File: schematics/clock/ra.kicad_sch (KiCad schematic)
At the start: 19 parts, among them U7 74LS173, U8 74LS173, U9 74LS245

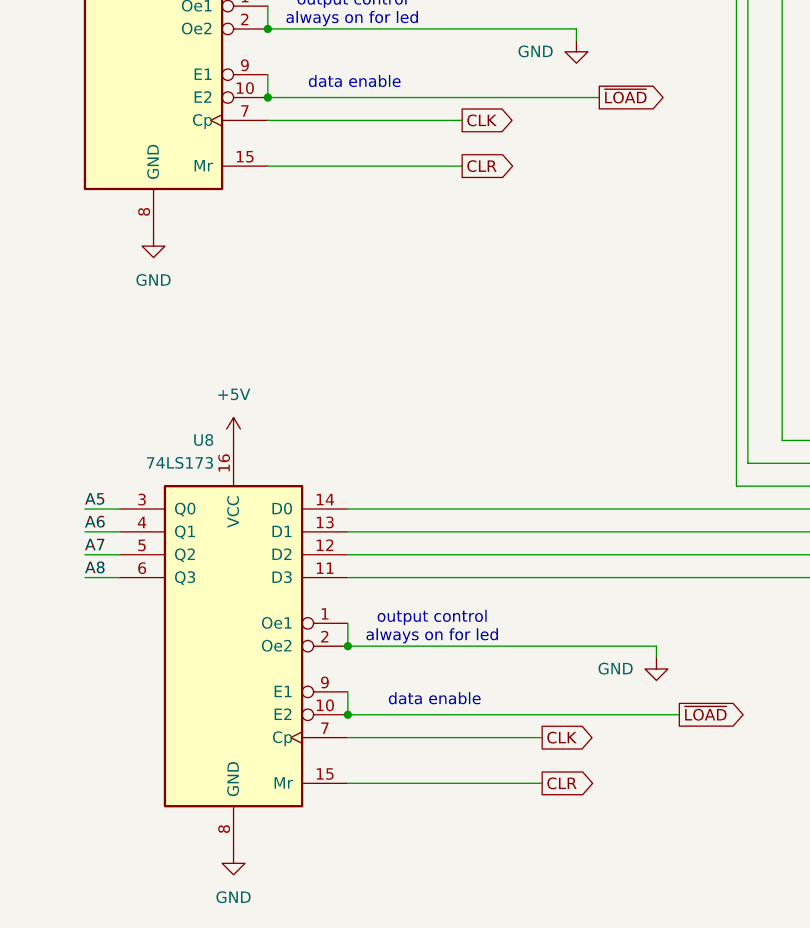
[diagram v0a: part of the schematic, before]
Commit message: ground clear
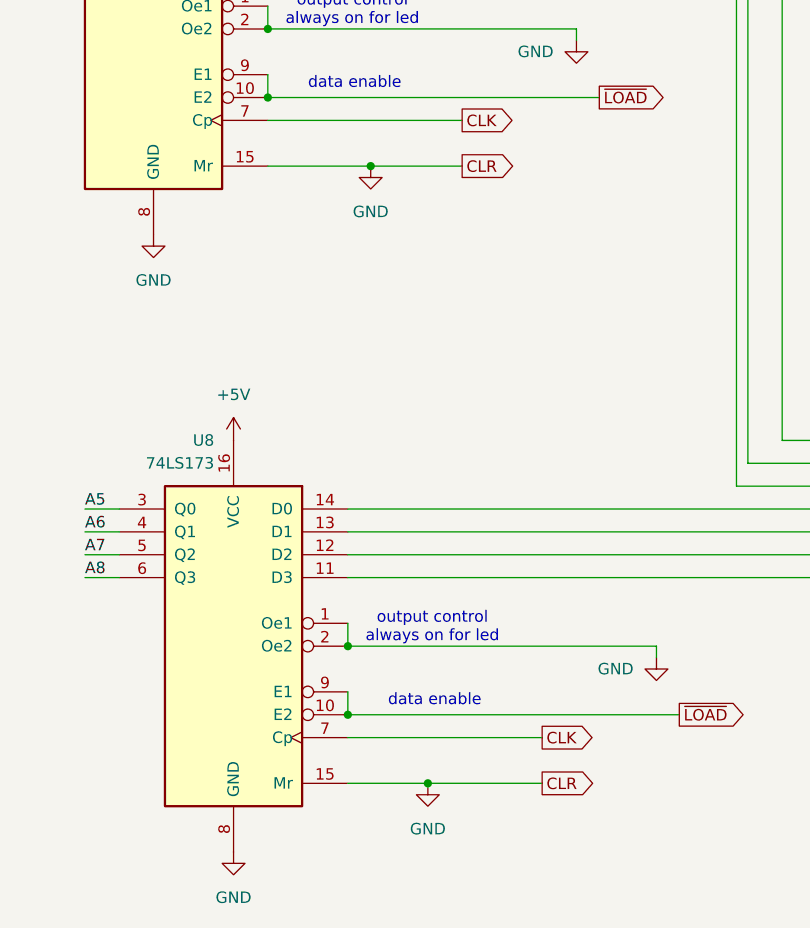
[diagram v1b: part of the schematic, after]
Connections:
- net CLR is gone; now on net GND: U7.15 (Mr), U8.15 (Mr)
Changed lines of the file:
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@@
 	)
 	(junction
+		(at 105.41 77.47)
+		(diameter 0)
+		(color 0 0 0 0)
+	)
+	(junction
 		(at 172.72 118.11)
 		(diameter 0)
@@
 	)
 	(junction
+		(at 111.76 146.05)
+		(diameter 0)
+		(color 0 0 0 0)
+	)
+	(junction
 		(at 185.42 60.96)
 		(diameter 0)
@@
 	(wire
 		(pts
+			(xy 111.76 146.05) (xy 102.87 146.05)
+		)
+		(stroke
+			(width 0)
+			(type default)
+		)
+	)
+	(wire
+		(pts
 			(xy 64.77 49.53) (xy 68.58 49.53)
 		)
@@
 	(wire
 		(pts
-			(xy 115.57 77.47) (xy 93.98 77.47)
+			(xy 115.57 77.47) (xy 105.41 77.47)
 		)
 		(stroke
@@
 	(wire
 		(pts
+			(xy 105.41 77.47) (xy 93.98 77.47)
+		)
+		(stroke
+			(width 0)
+			(type default)
+		)
+	)
+	(wire
+		(pts
 			(xy 179.07 60.96) (xy 185.42 60.96)
 		)
@@
 	(wire
 		(pts
-			(xy 124.46 146.05) (xy 102.87 146.05)
+			(xy 124.46 146.05) (xy 111.76 146.05)
 		)
 		(stroke
@@
 	)
 	(symbol
+		(lib_id "power:GND")
+		(at 111.76 146.05 0)
+		(unit 1)
+		(exclude_from_sim no)
+		(in_bom yes)
+		(on_board yes)
+		(dnp no)
+		(fields_autoplaced yes)
+		(property "Reference" "#PWR041"
+			(at 111.76 152.4 0)
+			(effects
+				(font
+					(size 1.27 1.27)
+				)
+				(hide yes)
+			)
+		)
+		(property "Value" "GND"
+			(at 111.76 151.13 0)
+			(effects
+				(font
+					(size 1.27 1.27)
+				)
+			)
+		)
+		(property "Footprint" ""
+			(at 111.76 146.05 0)
+			(effects
+				(font
+					(size 1.27 1.27)
+				)
+				(hide yes)
+			)
+		)
+		(property "Datasheet" ""
+			(at 111.76 146.05 0)
+			(effects
+				(font
+					(size 1.27 1.27)
+				)
+				(hide yes)
+			)
+		)
+		(property "Description" "Power symbol creates a global label with name \"GND\" , ground"
+			(at 111.76 146.05 0)
+			(effects
+				(font
+					(size 1.27 1.27)
+				)
+				(hide yes)
+			)
+		)
+		(pin "1"
+		)
+		(instances
+			(project "clock"
+				(path "/1be175cd-1437-4d72-8152-541f02e1a99b/d58d7b4b-c7c9-4a9b-82e5-f70bb60ff1ca/3d0a87ec-a2f4-438c-aa57-9e074d6f2ca0"
+					(reference "#PWR041")
+					(unit 1)
+				)
+			)
+		)
+	)
+	(symbol
 		(lib_id "Device:LED")
 		(at 179.07 78.74 270)
@@
 					(unit 1)
 				)
+			)
+		)
+	)
+	(symbol
+		(lib_id "power:GND")
+		(at 105.41 77.47 0)
+		(unit 1)
+		(exclude_from_sim no)
+		(in_bom yes)
+		(on_board yes)
+		(dnp no)
+		(fields_autoplaced yes)
+		(property "Reference" "#PWR040"
+			(at 105.41 83.82 0)
+			(effects
+				(font
+					(size 1.27 1.27)
+				)
+				(hide yes)
+			)
+		)
+		(property "Value" "GND"
+			(at 105.41 82.55 0)
+			(effects
+				(font
+					(size 1.27 1.27)
+				)
+			)
+		)
+		(property "Footprint" ""
+			(at 105.41 77.47 0)
+			(effects
+				(font
+					(size 1.27 1.27)
+				)
+				(hide yes)
+			)
+		)
+		(property "Datasheet" ""
+			(at 105.41 77.47 0)
+			(effects
+				(font
+					(size 1.27 1.27)
+				)
+				(hide yes)
+			)
+		)
+		(property "Description" "Power symbol creates a global label with name \"GND\" , ground"
+			(at 105.41 77.47 0)
+			(effects
+				(font
+					(size 1.27 1.27)
+				)
+				(hide yes)
+			)
+		)
+		(pin "1"
+		)
+		(instances
+			(project "clock"
+				(path "/1be175cd-1437-4d72-8152-541f02e1a99b/d58d7b4b-c7c9-4a9b-82e5-f70bb60ff1ca/3d0a87ec-a2f4-438c-aa57-9e074d6f2ca0"
+					(reference "#PWR040")
+					(unit 1)
+				)

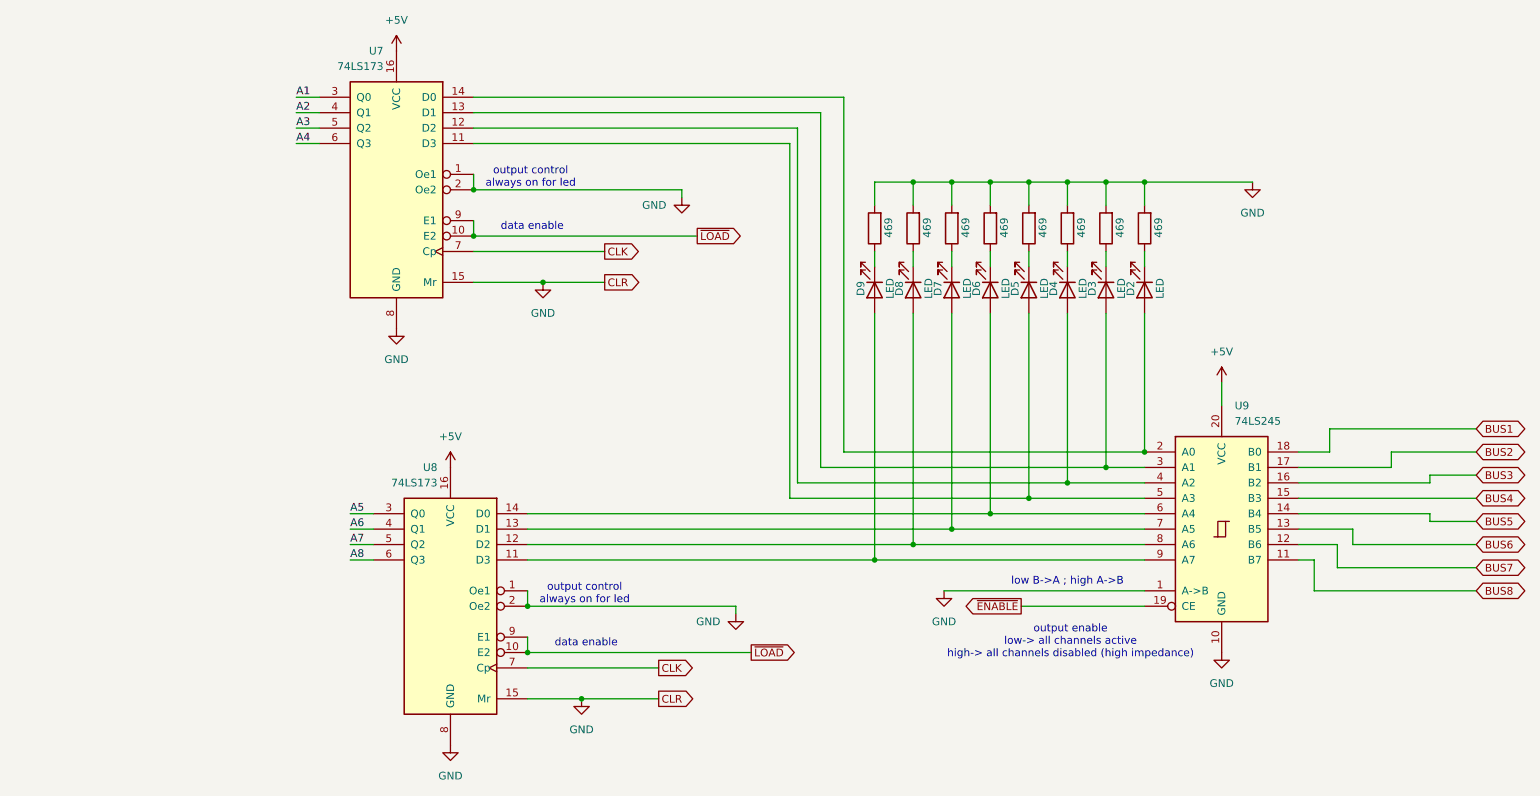
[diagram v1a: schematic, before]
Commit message: swap led position on registers
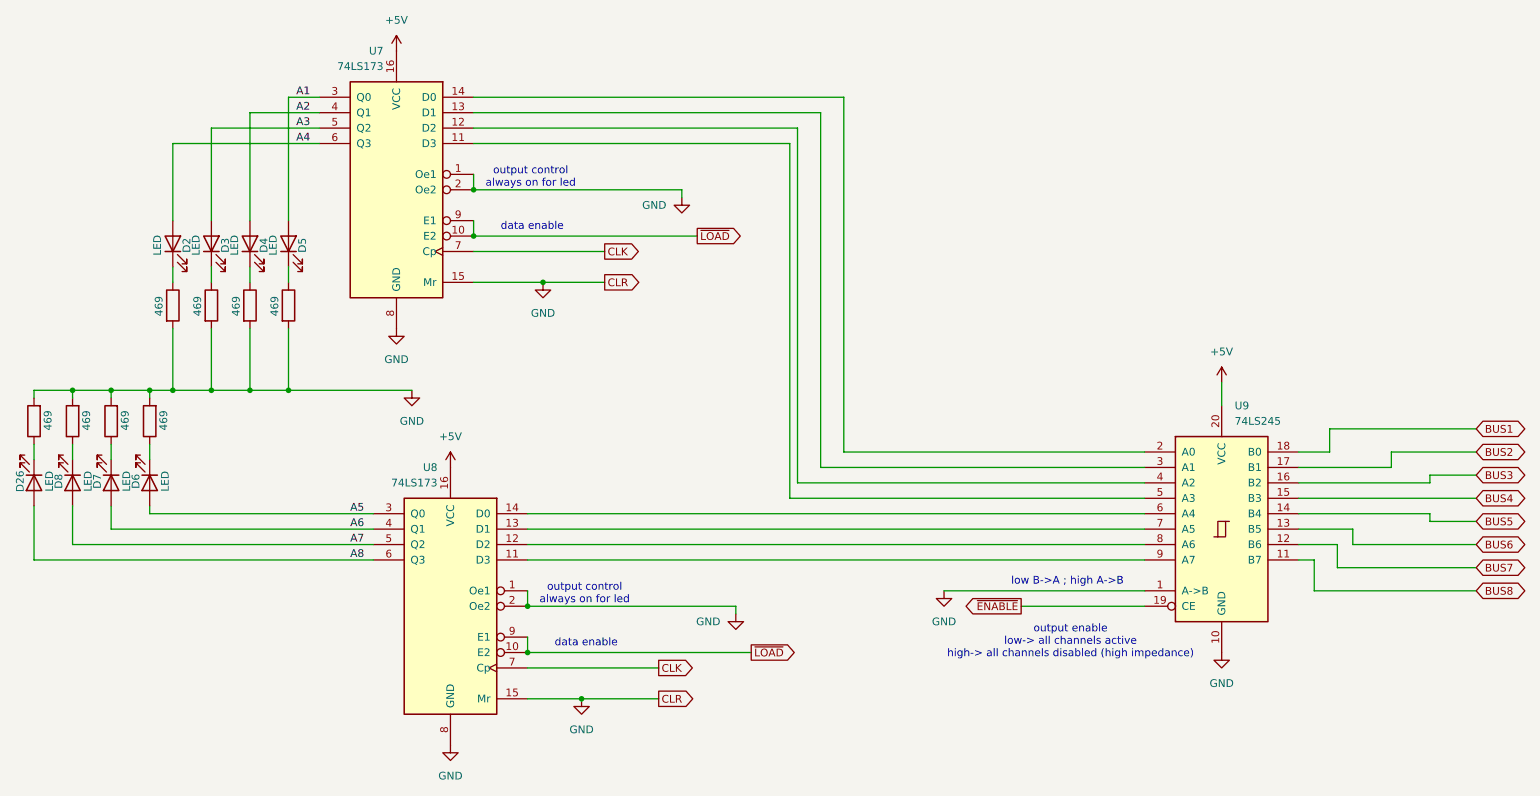
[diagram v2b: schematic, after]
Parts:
- removed D9: LED, symbol Device:LED
- removed RLED8: 469, symbol Device:R
- added D26: LED, symbol Device:LED
- added RLED33: 469, symbol Device:R
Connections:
- net A1: now also D5.2 (A)
- net A2: now also D4.2 (A)
- net A3: now also D3.2 (A)
- net A4: now also D2.2 (A)
- net A5: now also D6.2 (A)
- net A6: now also D7.2 (A)
- net A7: now also D8.2 (A)
- net A8: now also D26.2 (A)
- net GND: now also RLED33.2
- net at U7.11 (D3), U9.5 (A3): no longer D5.2 (A)
- net at U7.12 (D2), U9.4 (A2): no longer D4.2 (A)
- net at U7.13 (D1), U9.3 (A1): no longer D3.2 (A)
- net at U7.14 (D0), U9.2 (A0): no longer D2.2 (A)
- net at U8.12 (D2), U9.8 (A6): no longer D8.2 (A)
- net at U8.13 (D1), U9.7 (A5): no longer D7.2 (A)
- net at U8.14 (D0), U9.6 (A4): no longer D6.2 (A)
- new net: D26.1 (K), RLED33.1
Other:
- moved on the sheet: D2, D3, D4, D5, D6, D7, D8

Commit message: add alu
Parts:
- renumbered D5 to D18, D26 to D2, D8 to D3, D7 to D4, D6 to D5, D2 to D6, D3 to D7, D4 to D8, RLED33 to RLED1, RLED7 to RLED2, RLED4 to RLED25, RLED6 to RLED3, RLED5 to RLED4, RLED1 to RLED5, RLED2 to RLED6, RLED3 to RLED7
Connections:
- net ~{ENABLE} renamed enable
- net ~{LOAD} renamed load
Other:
- note added: "clear"

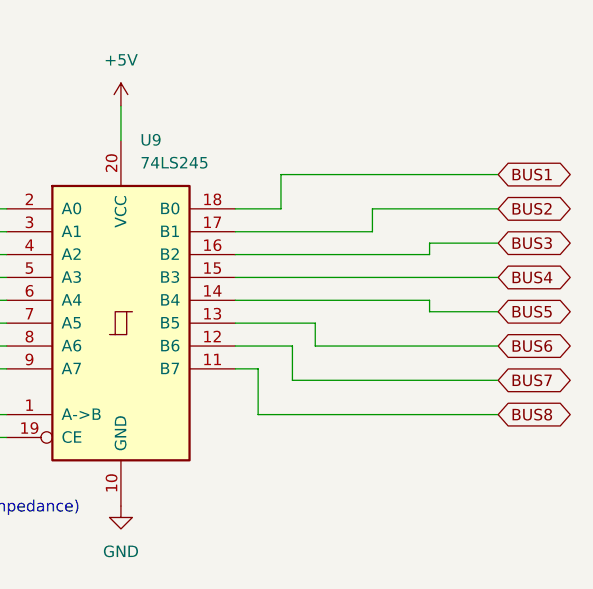
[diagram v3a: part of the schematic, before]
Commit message: add ram, change bus
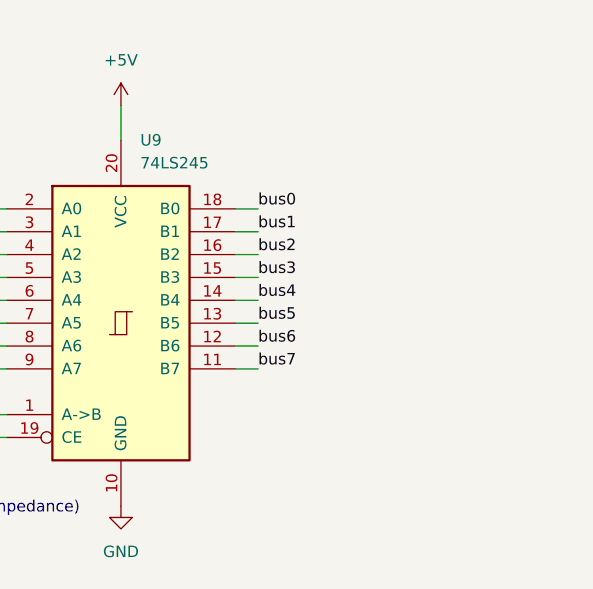
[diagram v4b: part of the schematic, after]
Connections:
- net BUS1 renamed bus0
- net BUS2 renamed bus1
- net BUS3 renamed bus2
- net BUS4 renamed bus3
- net BUS5 renamed bus4
- net BUS6 renamed bus5
- net BUS7 renamed bus6
- net BUS8 renamed bus7
